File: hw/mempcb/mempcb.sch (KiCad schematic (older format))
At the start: 31 parts, among them J1 RC6502_Bus, J2 0.1\" 2x25, U3 JEDEC_DIP32_RAM, U4 74LS138, U5 74LS138

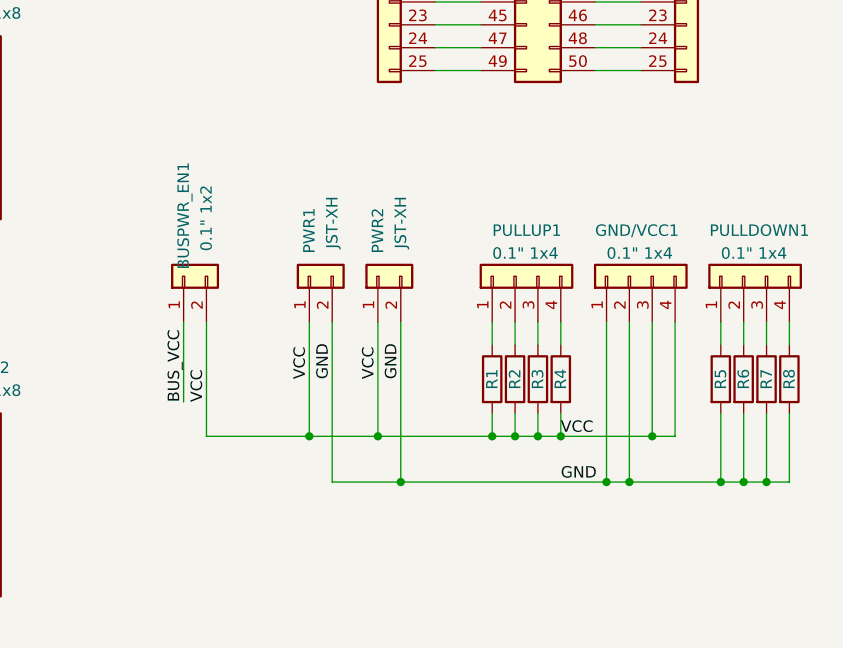
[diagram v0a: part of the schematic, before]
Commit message: hw/mempcb: New GND/Vcc WW pins: 4×GND, 2×Vcc, side by side w/buspwr jumper
The BUS_VCC jumper is now directly above the RC6502 bus Vcc pins, and the
two wire-wrap Vcc pins are directly above that. Directly to its right,
above the RC6502 bus GND, we have four wire-wrap pins for GND. (These
latter have traces on the bottom just to make this easier to recognise when
looking at the backside; they still should be connected to the top ground
fill when we get to that.)

These and the pull-up wire-wrap headers are oriented vertically to make
routing of wire-wrap easier.

All of these, including the pull-ups, are now routed.
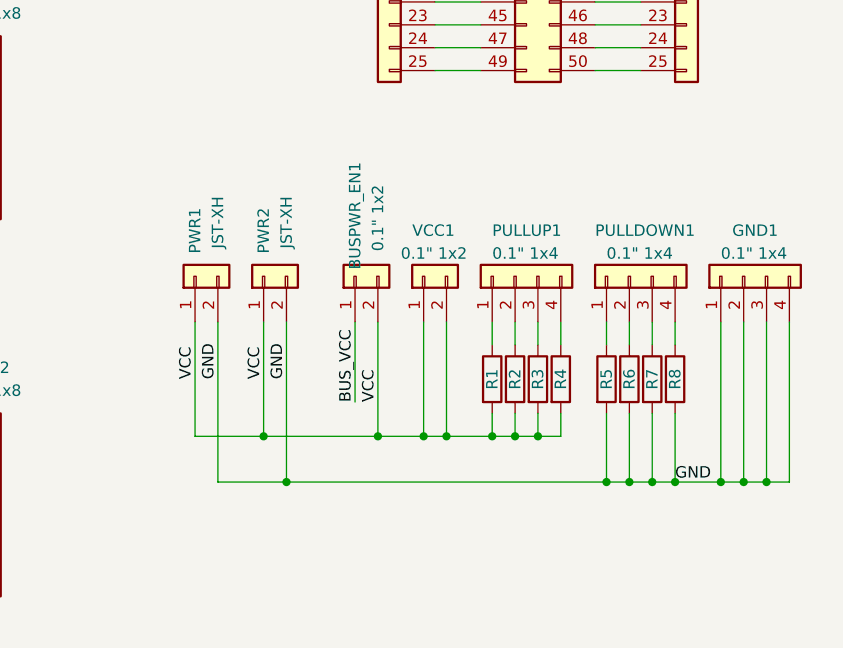
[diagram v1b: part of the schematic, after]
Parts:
- added VCC1: 0.1\" 1x2, Connector_PinHeader_2.54mm:PinHeader_1x02_P2.54mm_Vertical, symbol mempcb-rescue:Conn_01x02-Connector_Generic
- renumbered GND/VCC1 to GND1
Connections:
- net GND: now also GND1.3 (Pin_3), GND1.4 (Pin_4)
- net VCC: now also VCC1.1 (Pin_1), VCC1.2 (Pin_2); no longer GND1.3 (Pin_3), GND1.4 (Pin_4)
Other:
- moved on the sheet: BUSPWR_EN1, GND1, PULLDOWN1, PWR1, PWR2, R5, R6, R7, R8
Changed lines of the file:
@@
 VCC
 $Comp
-L mempcb-rescue:Conn_01x04-Connector_Generic GND/VCC1
+L mempcb-rescue:Conn_01x04-Connector_Generic GND1
 U 1 1 5FED18C8
-P 9300 4850
-F 0 "GND/VCC1" V 9500 5000 50  0000 R CNN
-F 1 "0.1\" 1x4" V 9400 4950 50  0000 R CNN
-F 2 "Connector_PinHeader_2.54mm:PinHeader_1x04_P2.54mm_Vertical" H 9300 4850 50  0001 C CNN
-F 3 "~" H 9300 4850 50  0001 C CNN
-	1    9300 4850
+P 9800 4850
+F 0 "GND1" V 10000 4900 50  0000 R CNN
+F 1 "0.1\" 1x4" V 9900 4950 50  0000 R CNN
+F 2 "Connector_PinHeader_2.54mm:PinHeader_1x04_P2.54mm_Vertical" H 9800 4850 50  0001 C CNN
+F 3 "~" H 9800 4850 50  0001 C CNN
+	1    9800 4850
 	0    -1   -1   0
 $EndComp
@@
 L mempcb-rescue:Conn_01x04-Connector_Generic PULLDOWN1
 U 1 1 6042687B
-P 9800 4850
-F 0 "PULLDOWN1" V 10000 5000 50  0000 R CNN
-F 1 "0.1\" 1x4" V 9900 4950 50  0000 R CNN
-F 2 "Connector_PinHeader_2.54mm:PinHeader_1x04_P2.54mm_Vertical" H 9800 4850 50  0001 C CNN
-F 3 "~" H 9800 4850 50  0001 C CNN
-	1    9800 4850
+P 9300 4850
+F 0 "PULLDOWN1" V 9500 5000 50  0000 R CNN
+F 1 "0.1\" 1x4" V 9400 4950 50  0000 R CNN
+F 2 "Connector_PinHeader_2.54mm:PinHeader_1x04_P2.54mm_Vertical" H 9300 4850 50  0001 C CNN
+F 3 "~" H 9300 4850 50  0001 C CNN
+	1    9300 4850
 	0    -1   -1   0
 $EndComp
@@
 L mempcb-rescue:R-Device R5
 U 1 1 60426881
-P 9700 5300
-F 0 "R5" V 9700 5300 50  0000 C CNN
-F 1 "R" V 9700 5300 50  0001 C CNN
-F 2 "Resistor_THT:R_Axial_DIN0207_L6.3mm_D2.5mm_P10.16mm_Horizontal" V 9630 5300 50  0001 C CNN
-F 3 "~" H 9700 5300 50  0001 C CNN
-	1    9700 5300
-	1    0    0    -1
-$EndComp
-Wire Wire Line
-	9700 5150 9700 5050
+P 9200 5300
+F 0 "R5" V 9200 5300 50  0000 C CNN
+F 1 "R" V 9200 5300 50  0001 C CNN
+F 2 "Resistor_THT:R_Axial_DIN0207_L6.3mm_D2.5mm_P10.16mm_Horizontal" V 9130 5300 50  0001 C CNN
+F 3 "~" H 9200 5300 50  0001 C CNN
+	1    9200 5300
+	1    0    0    -1
+$EndComp
+Wire Wire Line
+	9200 5150 9200 5050
 $Comp
 L mempcb-rescue:R-Device R6
 U 1 1 60426889
-P 9800 5300
-F 0 "R6" V 9800 5300 50  0000 C CNN
-F 1 "R" V 9800 5300 50  0001 C CNN
-F 2 "Resistor_THT:R_Axial_DIN0207_L6.3mm_D2.5mm_P10.16mm_Horizontal" V 9730 5300 50  0001 C CNN
-F 3 "~" H 9800 5300 50  0001 C CNN
-	1    9800 5300
-	1    0    0    -1
-$EndComp
-Wire Wire Line
-	9800 5150 9800 5050
+P 9300 5300
+F 0 "R6" V 9300 5300 50  0000 C CNN
+F 1 "R" V 9300 5300 50  0001 C CNN
+F 2 "Resistor_THT:R_Axial_DIN0207_L6.3mm_D2.5mm_P10.16mm_Horizontal" V 9230 5300 50  0001 C CNN
+F 3 "~" H 9300 5300 50  0001 C CNN
+	1    9300 5300
+	1    0    0    -1
+$EndComp
+Wire Wire Line
+	9300 5150 9300 5050
 $Comp
 L mempcb-rescue:R-Device R7
 U 1 1 60426891
-P 9900 5300
-F 0 "R7" V 9900 5300 50  0000 C CNN
-F 1 "R" V 9900 5300 50  0001 C CNN
-F 2 "Resistor_THT:R_Axial_DIN0207_L6.3mm_D2.5mm_P10.16mm_Horizontal" V 9830 5300 50  0001 C CNN
-F 3 "~" H 9900 5300 50  0001 C CNN
-	1    9900 5300
-	1    0    0    -1
-$EndComp
-Wire Wire Line
-	9900 5150 9900 5050
+P 9400 5300
+F 0 "R7" V 9400 5300 50  0000 C CNN
+F 1 "R" V 9400 5300 50  0001 C CNN
+F 2 "Resistor_THT:R_Axial_DIN0207_L6.3mm_D2.5mm_P10.16mm_Horizontal" V 9330 5300 50  0001 C CNN
+F 3 "~" H 9400 5300 50  0001 C CNN
+	1    9400 5300
+	1    0    0    -1
+$EndComp
+Wire Wire Line
+	9400 5150 9400 5050
 $Comp
 L mempcb-rescue:R-Device R8
 U 1 1 60426899
-P 10000 5300
-F 0 "R8" V 10000 5300 50  0000 C CNN
-F 1 "R" V 10000 5300 50  0001 C CNN
-F 2 "Resistor_THT:R_Axial_DIN0207_L6.3mm_D2.5mm_P10.16mm_Horizontal" V 9930 5300 50  0001 C CNN
-F 3 "~" H 10000 5300 50  0001 C CNN
-	1    10000 5300
-	1    0    0    -1
-$EndComp
-Wire Wire Line
-	10000 5150 10000 5050
-Connection ~ 9000 5550
-Text Label 9000 5550 0    50   ~ 0
-VCC
+P 9500 5300
+F 0 "R8" V 9500 5300 50  0000 C CNN
+F 1 "R" V 9500 5300 50  0001 C CNN
+F 2 "Resistor_THT:R_Axial_DIN0207_L6.3mm_D2.5mm_P10.16mm_Horizontal" V 9430 5300 50  0001 C CNN
+F 3 "~" H 9500 5300 50  0001 C CNN
+	1    9500 5300
+	1    0    0    -1
+$EndComp
+Wire Wire Line
+	9500 5150 9500 5050
 $Comp
 L mempcb-rescue:R-Device R1
@@
 L mempcb-rescue:Conn_01x02-Connector_Generic PWR1
 U 1 1 604FEFCF
-P 7900 4850
-F 0 "PWR1" H 8200 4850 50  0000 R CNN
-F 1 "JST-XH" H 8250 4750 50  0000 R CNN
-F 2 "Connector_JST:JST_XH_B2B-XH-A_1x02_P2.50mm_Vertical" H 7900 4850 50  0001 C CNN
-F 3 "~" H 7900 4850 50  0001 C CNN
-	1    7900 4850
-	0    -1   -1   0
-$EndComp
-Text Label 7900 5300 1    50   ~ 0
-VCC
-Text Label 8000 5300 1    50   ~ 0
-GND
+P 7400 4850
+F 0 "PWR1" H 7700 4850 50  0000 R CNN
+F 1 "JST-XH" H 7750 4750 50  0000 R CNN
+F 2 "Connector_JST:JST_XH_B2B-XH-A_1x02_P2.50mm_Vertical" H 7400 4850 50  0001 C CNN
+F 3 "~" H 7400 4850 50  0001 C CNN
+	1    7400 4850
+	0    -1   -1   0
+$EndComp
 $Comp
 L mempcb-rescue:Conn_01x02-Connector_Generic PWR2
 U 1 1 6051B38D
-P 8200 4850
-F 0 "PWR2" H 8500 4850 50  0000 R CNN
-F 1 "JST-XH" H 8550 4750 50  0000 R CNN
-F 2 "Connector_JST:JST_XH_B2B-XH-A_1x02_P2.50mm_Vertical" H 8200 4850 50  0001 C CNN
-F 3 "~" H 8200 4850 50  0001 C CNN
-	1    8200 4850
-	0    -1   -1   0
-$EndComp
-Text Label 8200 5300 1    50   ~ 0
+P 7700 4850
+F 0 "PWR2" H 8000 4850 50  0000 R CNN
+F 1 "JST-XH" H 8050 4750 50  0000 R CNN
+F 2 "Connector_JST:JST_XH_B2B-XH-A_1x02_P2.50mm_Vertical" H 7700 4850 50  0001 C CNN
+F 3 "~" H 7700 4850 50  0001 C CNN
+	1    7700 4850
+	0    -1   -1   0
+$EndComp
+Text Label 7700 5300 1    50   ~ 0
 VCC
-Text Label 8300 5300 1    50   ~ 0
+Text Label 7800 5300 1    50   ~ 0
 GND
 Text Label 2100 2600 0    50   ~ 0
@@
 L mempcb-rescue:Conn_01x02-Connector_Generic BUSPWR_EN1
 U 1 1 60556D43
-P 7350 4850
-F 0 "BUSPWR_EN1" H 7850 4850 50  0000 R CNN
-F 1 "0.1\" 1x2" H 7750 4750 50  0000 R CNN
-F 2 "Connector_PinHeader_2.54mm:PinHeader_1x02_P2.54mm_Vertical" H 7350 4850 50  0001 C CNN
-F 3 "~" H 7350 4850 50  0001 C CNN
-	1    7350 4850
-	0    -1   -1   0
-$EndComp
-Text Label 7350 5400 1    50   ~ 0
+P 8100 4850
+F 0 "BUSPWR_EN1" H 8600 4850 50  0000 R CNN
+F 1 "0.1\" 1x2" H 8500 4750 50  0000 R CNN
+F 2 "Connector_PinHeader_2.54mm:PinHeader_1x02_P2.54mm_Vertical" H 8100 4850 50  0001 C CNN
+F 3 "~" H 8100 4850 50  0001 C CNN
+	1    8100 4850
+	0    -1   -1   0
+$EndComp
+Text Label 8100 5400 1    50   ~ 0
 BUS_VCC
 Wire Wire Line
-	7350 5050 7350 5400
-Text Label 7450 5400 1    50   ~ 0
+	8100 5050 8100 5400
+Text Label 8200 5400 1    50   ~ 0
 VCC
 Wire Wire Line
-	7450 5550 7900 5550
-Wire Wire Line
-	7450 5050 7450 5550
-Connection ~ 8700 5550
-Wire Wire Line
-	7900 5050 7900 5550
-Connection ~ 7900 5550
-Wire Wire Line
-	7900 5550 8200 5550
+	8200 5550 8400 5550
 Wire Wire Line
 	8200 5050 8200 5550
-Connection ~ 8200 5550
-Wire Wire Line
-	8200 5550 8700 5550
-Wire Wire Line
-	8000 5750 8300 5750
-Wire Wire Line
-	8000 5050 8000 5750
-Wire Wire Line
-	8300 5050 8300 5750
-Connection ~ 8300 5750
-Wire Wire Line
-	10000 5450 10000 5750
-Wire Wire Line
-	9900 5450 9900 5750
-Connection ~ 9900 5750
-Wire Wire Line
-	9900 5750 10000 5750
-Wire Wire Line
-	9800 5450 9800 5750
-Connection ~ 9800 5750
-Wire Wire Line
-	9800 5750 9900 5750
-Wire Wire Line
-	9700 5450 9700 5750
-Wire Wire Line
-	9700 5750 9800 5750
-Text Label 9000 5750 0    50   ~ 0
+Wire Wire Line
+	7400 5050 7400 5550
+Wire Wire Line
+	7400 5550 7700 5550
+Wire Wire Line
+	7700 5050 7700 5550
+Connection ~ 7700 5550
+Wire Wire Line
+	7700 5550 8200 5550
+Wire Wire Line
+	7500 5750 7800 5750
+Wire Wire Line
+	7500 5050 7500 5750
+Wire Wire Line
+	7800 5050 7800 5750
+Connection ~ 7800 5750
+Wire Wire Line
+	9500 5450 9500 5750
+Wire Wire Line
+	9400 5450 9400 5750
+Wire Wire Line
+	9300 5450 9300 5750
+Wire Wire Line
+	9200 5450 9200 5750
+Text Label 9500 5750 0    50   ~ 0
 GND
 Wire Wire Line
@@
 $EndComp
 Wire Wire Line
-	8300 5750 9200 5750
-Wire Wire Line
-	9500 5550 9500 5050
-Wire Wire Line
-	9000 5550 9400 5550
-Wire Wire Line
-	9400 5050 9400 5550
-Connection ~ 9400 5550
-Wire Wire Line
-	9400 5550 9500 5550
-Wire Wire Line
-	9200 5050 9200 5750
-Connection ~ 9200 5750
-Wire Wire Line
-	9200 5750 9300 5750
-Wire Wire Line
-	9300 5050 9300 5750
-Wire Wire Line
-	9700 5750 9300 5750
-Connection ~ 9700 5750
-Connection ~ 9300 5750
+	9700 5050 9700 5750
+Wire Wire Line
+	9800 5050 9800 5750
 Text Label 4750 1700 0    50   ~ 0
 A7
+Wire Wire Line
+	9200 5750 9300 5750
+Connection ~ 9300 5750
+Wire Wire Line
+	9300 5750 9400 5750
+Connection ~ 9400 5750
+Wire Wire Line
+	9400 5750 9500 5750
+Wire Wire Line
+	10000 5050 10000 5750
+Wire Wire Line
+	10000 5750 9900 5750
+Connection ~ 9500 5750
+Connection ~ 9700 5750
+Wire Wire Line
+	9700 5750 9500 5750
+Connection ~ 9800 5750
+Wire Wire Line
+	9800 5750 9700 5750
+Wire Wire Line
+	9900 5050 9900 5750
+Connection ~ 9900 5750
+Wire Wire Line
+	9900 5750 9800 5750
+Connection ~ 8200 5550
+$Comp
+L mempcb-rescue:Conn_01x02-Connector_Generic VCC1
+U 1 1 5FFB1DFF
+P 8400 4850
+F 0 "VCC1" V 8600 4900 50  0000 R CNN
+F 1 "0.1\" 1x2" V 8500 4950 50  0000 R CNN
+F 2 "Connector_PinHeader_2.54mm:PinHeader_1x02_P2.54mm_Vertical" H 8400 4850 50  0001 C CNN
+F 3 "" H 8400 4850 50  0001 C CNN
+	1    8400 4850
+	0    -1   -1   0
+$EndComp
+Wire Wire Line
+	8400 5050 8400 5550
+Connection ~ 8400 5550
+Wire Wire Line
+	8400 5550 8500 5550
+Wire Wire Line
+	8500 5050 8500 5550
+Connection ~ 8500 5550
+Wire Wire Line
+	8500 5550 8700 5550
+Connection ~ 8700 5550
+Text Label 7500 5300 1    50   ~ 0
+GND
+Text Label 7400 5300 1    50   ~ 0
+VCC
+Wire Wire Line
+	7800 5750 9200 5750
+Connection ~ 9200 5750
 $EndSCHEMATC

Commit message: hw/mempcb: Change rescue symbols back to the normal ones
Revert "hw/mempcb sch: Save automatic changes from my first opening of this". This reverts commit 808559914cb61a0f7c65a8535ad7c551a7aa0b5a.
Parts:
- BUSPWR_EN1, PWR1, PWR2, VCC1: symbol mempcb-rescue:Conn_01x02-Connector_Generic -> Connector_Generic:Conn_01x02
- C1, C2, C3: symbol mempcb-rescue:C-Device -> Device:C
- GND1, PULLDOWN1, PULLUP1: symbol mempcb-rescue:Conn_01x04-Connector_Generic -> Connector_Generic:Conn_01x04
- J2: symbol mempcb-rescue:Conn_02x25_Odd_Even-Connector_Generic -> Connector_Generic:Conn_02x25_Odd_Even
- R1, R2, R3, R4, R5, R6, R7, R8: symbol mempcb-rescue:R-Device -> Device:R
- W2_1, W2_2: symbol mempcb-rescue:Conn_01x25-Connector_Generic -> Connector_Generic:Conn_01x25
- W3_1, W3_2: symbol mempcb-rescue:Conn_01x16-Connector_Generic -> Connector_Generic:Conn_01x16
- W4_1, W4_2, W5_1, W5_2: symbol mempcb-rescue:Conn_01x08-Connector_Generic -> Connector_Generic:Conn_01x08
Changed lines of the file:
@@
 EESchema Schematic File Version 4
-LIBS:mempcb-cache
-EELAYER 26 0
+EELAYER 30 0
 EELAYER END
 $Descr A4 11693 8268
@@
 $EndComp
 $Comp
-L mempcb-rescue:Conn_02x25_Odd_Even-Connector_Generic J2
+L Connector_Generic:Conn_02x25_Odd_Even J2
 U 1 1 5FEB0496
 P 8850 2750
@@
 $EndComp
 $Comp
-L mempcb-rescue:Conn_01x25-Connector_Generic W2_1
+L Connector_Generic:Conn_01x25 W2_1
 U 1 1 5FEB2EF1
 P 8250 2750
@@
 $EndComp
 $Comp
-L mempcb-rescue:Conn_01x25-Connector_Generic W2_2
+L Connector_Generic:Conn_01x25 W2_2
 U 1 1 5FEC1F3E
 P 9550 2750
@@
 $EndComp
 $Comp
-L mempcb-rescue:Conn_01x16-Connector_Generic W3_1
+L Connector_Generic:Conn_01x16 W3_1
 U 1 1 5FECEA90
 P 4550 2000
@@
 $EndComp
 $Comp
-L mempcb-rescue:Conn_01x08-Connector_Generic W4_2
+L Connector_Generic:Conn_01x08 W4_2
 U 1 1 5FECFD2E
 P 6500 4150
@@
 $EndComp
 $Comp
-L mempcb-rescue:Conn_01x08-Connector_Generic W4_1
+L Connector_Generic:Conn_01x08 W4_1
 U 1 1 5FED086C
 P 4500 4150
@@
 	6250 1300 6200 1300
 $Comp
-L mempcb-rescue:Conn_01x16-Connector_Generic W3_2
+L Connector_Generic:Conn_01x16 W3_2
 U 1 1 5FECF06C
 P 6450 2000
@@
 VCC
 $Comp
-L mempcb-rescue:Conn_01x04-Connector_Generic GND1
+L Connector_Generic:Conn_01x04 GND1
 U 1 1 5FED18C8
 P 9800 4850
@@
 $EndComp
 $Comp
-L mempcb-rescue:Conn_01x04-Connector_Generic PULLUP1
+L Connector_Generic:Conn_01x04 PULLUP1
 U 1 1 6032F1DA
 P 8800 4850
@@
 	8700 5150 8700 5050
 $Comp
-L mempcb-rescue:R-Device R2
+L Device:R R2
 U 1 1 603E796E
 P 8800 5300
@@
 	8800 5150 8800 5050
 $Comp
-L mempcb-rescue:R-Device R3
+L Device:R R3
 U 1 1 60400026
 P 8900 5300
@@
 	8900 5150 8900 5050
 $Comp
-L mempcb-rescue:R-Device R4
+L Device:R R4
 U 1 1 6040C3DC
 P 9000 5300
@@
 	8900 5550 9000 5550
 $Comp
-L mempcb-rescue:Conn_01x04-Connector_Generic PULLDOWN1
+L Connector_Generic:Conn_01x04 PULLDOWN1
 U 1 1 6042687B
 P 9300 4850
@@
 $EndComp
 $Comp
-L mempcb-rescue:R-Device R5
+L Device:R R5
 U 1 1 60426881
 P 9200 5300
@@
 	9200 5150 9200 5050
 $Comp
-L mempcb-rescue:R-Device R6
+L Device:R R6
 U 1 1 60426889
 P 9300 5300
@@
 	9300 5150 9300 5050
 $Comp
-L mempcb-rescue:R-Device R7
+L Device:R R7
 U 1 1 60426891
 P 9400 5300
@@
 	9400 5150 9400 5050
 $Comp
-L mempcb-rescue:R-Device R8
+L Device:R R8
 U 1 1 60426899
 P 9500 5300
@@
 	9500 5150 9500 5050
 $Comp
-L mempcb-rescue:R-Device R1
+L Device:R R1
 U 1 1 603CD90C
 P 8700 5300
@@
 $EndComp
 $Comp
-L mempcb-rescue:Conn_01x02-Connector_Generic PWR1
+L Connector_Generic:Conn_01x02 PWR1
 U 1 1 604FEFCF
 P 7400 4850
@@
 $EndComp
 $Comp
-L mempcb-rescue:Conn_01x02-Connector_Generic PWR2
+L Connector_Generic:Conn_01x02 PWR2
 U 1 1 6051B38D
 P 7700 4850
@@
 BUS_VCC
 $Comp
-L mempcb-rescue:Conn_01x02-Connector_Generic BUSPWR_EN1
+L Connector_Generic:Conn_01x02 BUSPWR_EN1
 U 1 1 60556D43
 P 8100 4850
@@
 	6050 3850 6300 3850
 $Comp
-L mempcb-rescue:C-Device C2
+L Device:C C2
 U 1 1 5FF0AFCA
 P 5500 5000
@@
 $EndComp
 $Comp
-L mempcb-rescue:C-Device C1
+L Device:C C1
 U 1 1 5FF2C1A0
 P 5500 3200
@@
 	6200 1300 6000 1300
 $Comp
-L mempcb-rescue:Conn_01x08-Connector_Generic W5_2
+L Connector_Generic:Conn_01x08 W5_2
 U 1 1 5FF51E6E
 P 6500 5800
@@
 $EndComp
 $Comp
-L mempcb-rescue:Conn_01x08-Connector_Generic W5_1
+L Connector_Generic:Conn_01x08 W5_1
 U 1 1 5FF51E74
 P 4500 5800
@@
 	6050 5500 6300 5500
 $Comp
-L mempcb-rescue:C-Device C3
+L Device:C C3
 U 1 1 5FF51E9A
 P 5500 6650
@@
 Connection ~ 8200 5550
 $Comp
-L mempcb-rescue:Conn_01x02-Connector_Generic VCC1
+L Connector_Generic:Conn_01x02 VCC1
 U 1 1 5FFB1DFF
 P 8400 4850

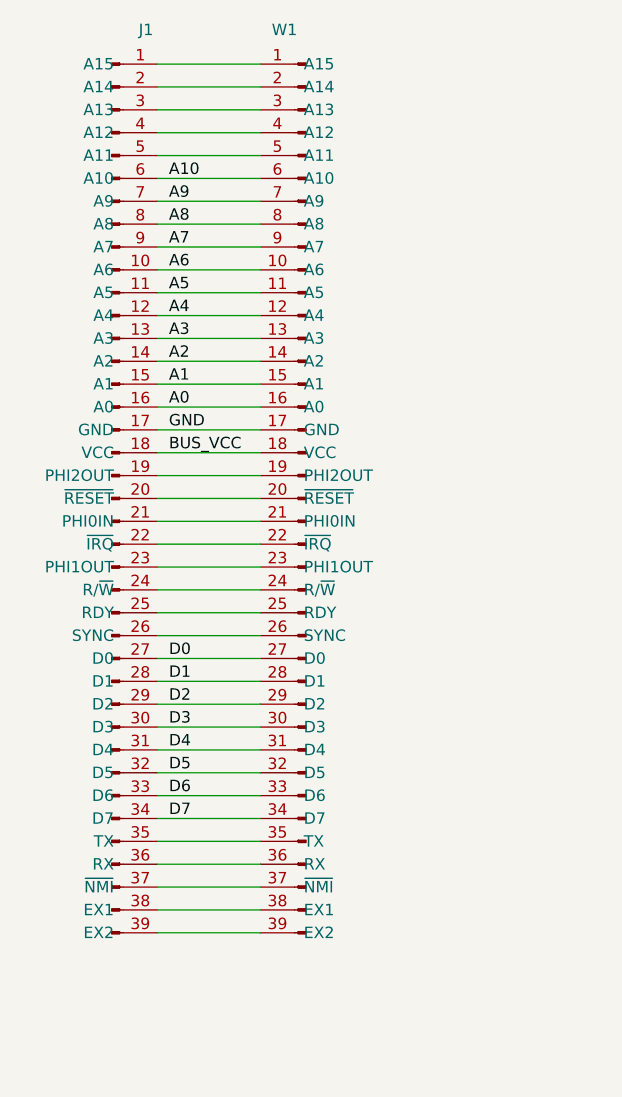
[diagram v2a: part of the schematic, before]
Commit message: hw/mempcb: Label all bus nets
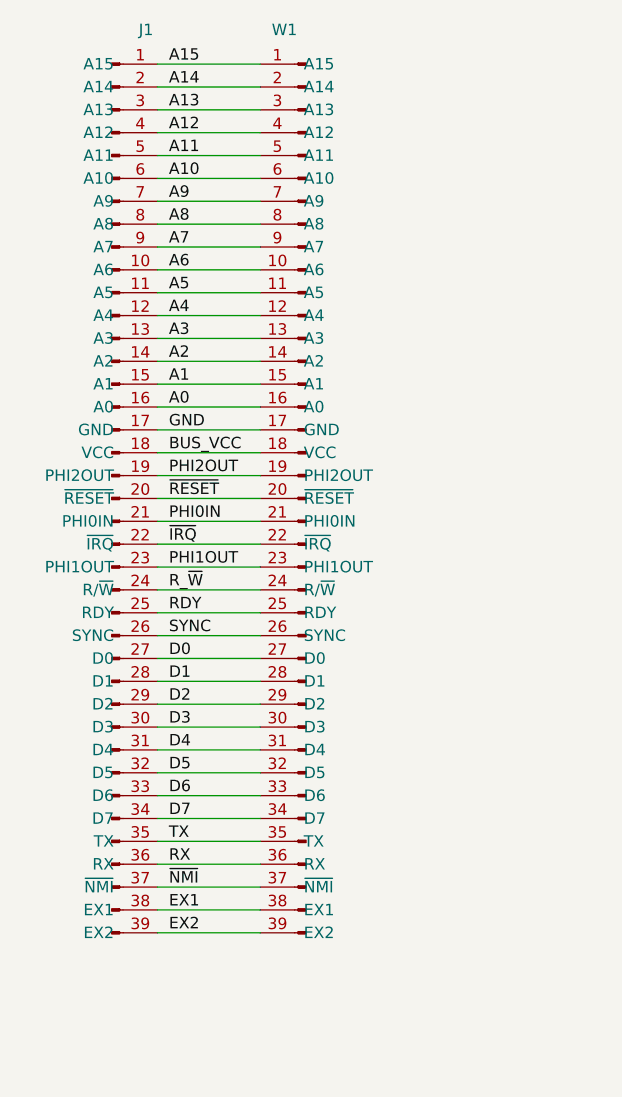
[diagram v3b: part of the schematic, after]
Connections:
- net A15: now reaches J1.1 (A15), W1.1 (A15)
- net PHI2OUT: now reaches J1.19 (PHI2OUT), W1.19 (PHI2OUT)
- net A14: now reaches J1.2 (A14), W1.2 (A14)
- net ~RESET: now reaches J1.20 (~RESET), W1.20 (~RESET)
- net PHI0IN: now reaches J1.21 (PHI0IN), W1.21 (PHI0IN)
- net ~IRQ: now reaches J1.22 (~IRQ), W1.22 (~IRQ)
- net PHI1OUT: now reaches J1.23 (PHI1OUT), W1.23 (PHI1OUT)
- net R_~W: now reaches J1.24 (R/~W), W1.24 (R/~W)
- net RDY: now reaches J1.25 (RDY), W1.25 (RDY)
- net SYNC: now reaches J1.26 (SYNC), W1.26 (SYNC)
- net A13: now reaches J1.3 (A13), W1.3 (A13)
- net TX: now reaches J1.35 (TX), W1.35 (TX)
- net RX: now reaches J1.36 (RX), W1.36 (RX)
- net ~NMI: now reaches J1.37 (~NMI), W1.37 (~NMI)
- net EX1: now reaches J1.38 (EX1), W1.38 (EX1)
- net EX2: now reaches J1.39 (EX2), W1.39 (EX2)
- net A12: now reaches J1.4 (A12), W1.4 (A12)
- net A11: now reaches J1.5 (A11), W1.5 (A11)
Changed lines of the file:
@@
 	7800 5750 9200 5750
 Connection ~ 9200 5750
+Text Label 2100 1400 0    50   ~ 0
+A11
+Text Label 2100 1300 0    50   ~ 0
+A12
+Text Label 2100 1200 0    50   ~ 0
+A13
+Text Label 2100 1100 0    50   ~ 0
+A14
+Text Label 2100 1000 0    50   ~ 0
+A15
+Text Label 2100 2800 0    50   ~ 0
+PHI2OUT
+Text Label 2100 2900 0    50   ~ 0
+~RESET
+Text Label 2100 3000 0    50   ~ 0
+PHI0IN
+Text Label 2100 3100 0    50   ~ 0
+~IRQ
+Text Label 2100 3200 0    50   ~ 0
+PHI1OUT
+Text Label 2100 3300 0    50   ~ 0
+R_~W
+Text Label 2100 3400 0    50   ~ 0
+RDY
+Text Label 2100 3500 0    50   ~ 0
+SYNC
+Text Label 2100 4400 0    50   ~ 0
+TX
+Text Label 2100 4500 0    50   ~ 0
+RX
+Text Label 2100 4600 0    50   ~ 0
+~NMI
+Text Label 2100 4700 0    50   ~ 0
+EX1
+Text Label 2100 4800 0    50   ~ 0
+EX2
 $EndSCHEMATC
